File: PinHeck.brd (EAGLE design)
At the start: 359.2 x 152.3 mm, 309 parts, among them IC1 FT232RQ, IC2 PIC32MX7X5FL-PT, IC3 CD74HCT244E, IC4 CD74HCT244E, IC5 ULN2803A, J1 500075-1517, J11 No Load, J2 500075-1517, J6 161-3507-E, SW1 101-0134-EV, SW2 101-0134-EV, U1 P8X32A-Q44, U10 74HCT2G04GV,125, U11 74HC165D,652, U12 74HC165D,652, U13 MIC1232, U14 MC74HC08ADG, U15 MC74HC08ADG, U16 MC74HC08ADG, U17 MC74HC08ADG, U18 MC74HC08ADG, U19 MC74HC08ADG, U2 FT230X, U20 TIP107, U21 TIP107, U22 TIP107, U23 TIP107, U24 TIP107, U25 TIP107, U26 TIP107, U27 TIP107, U28 TIP102, U29 TIP102, U3 74HC595D-Q100, U30 TIP102, U31 TIP102, U32 TIP102, U33 TIP102, U34 TIP102, U35 TIP102, U36 WS2801, U37 TIP102, U38 WS2801, U4 CAT24M01XI-T2, U5 74HC595D-Q100, U6 74HC595D-Q100, U7 74HC595D-Q100, U8 74HC595D-Q100, U9 74HC595D-Q100, X1 FQ7050B-8.000, X2 ECS-65-20-4X

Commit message: Changed the alphanumeric display to be GI.
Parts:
- removed AN_J3, AN_J6, AN_J7: 26-60-4090, PP_Connectors:MOLEX_KK_9
- removed C27, C28, C29, C30, C31: .1uF, PP_Passives:0805
- removed MPU: (no value), PP_Connectors:HEADER_02X13_PTH
- added GI_0, GI_1: 26-60-4090, PP_Connectors:MOLEX_KK_9
- added R101, R103, R105, R107, R109, R111, R113, R125, R126, R127, R128, R129, R130, R131, R132, R99: 360, PP_Passives:0805
- added U40, U41, U42, U43, U44, U45, U46, U47, U48, U49, U50, U51: TIP102, PP_DiscreteSemi:TO-220AB
- SOL_0, SOL_1, SOL_10, SOL_11, SOL_12, SOL_13, SOL_14, SOL_15, SOL_16, SOL_17, SOL_18, SOL_19, SOL_2, SOL_20, SOL_21, SOL_22, SOL_23, SOL_3, SOL_4, SOL_5, SOL_6, SOL_7, SOL_8, SOL_9: value RFP12N10L -> IRL530
- U6, U7, U8, U9: value 74HC595D-Q100 -> TIP102; device PP_DigitalIC:SO-16 -> PP_DiscreteSemi:TO-220AB
- moved U5 35.2 mm to (308.6, 57.7), turned to 0 degrees
- moved U3 25.9 mm to (308.6, 98.6)
- moved C26 25.2 mm to (301.0, 57.1)
- moved U7 23.9 mm to (290.3, 80.5), turned to 90 degrees
- moved U8 23.9 mm to (296.7, 80.5), turned to 90 degrees
- moved C25 18.9 mm to (301.8, 99.3), turned to 90 degrees
- moved U6 12.7 mm to (284.0, 80.5), turned to 90 degrees
- moved U9 11.9 mm to (303.3, 80.5), turned to 90 degrees
- moved U10 8.44 mm to (289.1, 101.6), turned to 180 degrees
- moved U20 1.27 mm to (-5.59, 93.2)
- moved U22 1.27 mm to (4.06, 93.2)
- moved U24 1.27 mm to (13.7, 93.2)
- moved U26 1.27 mm to (23.4, 93.2)
- moved U28 1.02 mm to (-5.84, 48.3)
- moved U30 1.02 mm to (3.81, 48.3)
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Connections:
- net AN_DATA_COL renamed GI_DATA_COL
- net AN_DATA_COL_B renamed GI_DATA_COL_B
- removed net AN_J3_1: AN_J3.P$1, U5.7
- removed net AN_J3_2: AN_J3.P$2, U5.6
- removed net AN_J3_3: AN_J3.P$3, U5.5
- removed net AN_J3_4: AN_J3.P$4, U5.4
- removed net AN_J3_5: AN_J3.P$5, U5.3
- removed net AN_J3_6: AN_J3.P$6, U5.2
- removed net AN_J3_7: AN_J3.P$8, U5.1
- removed net AN_J3_8: AN_J3.P$9, U5.15
- removed net AN_J6_1: AN_J6.P$1, U3.7
- removed net AN_J6_2: AN_J6.P$2, U3.6
- removed net AN_J6_3: AN_J6.P$3, U3.5
- removed net AN_J6_4: AN_J6.P$4, U3.4
- removed net AN_J6_5: AN_J6.P$5, U3.3
- removed net AN_J6_6: AN_J6.P$6, U3.2
- removed net AN_J6_7: AN_J6.P$7, U3.1
- removed net AN_J6_8: AN_J6.P$9, U3.15
- removed net AN_J7_1: AN_J7.P$1, U6.15
- removed net AN_J7_2: AN_J7.P$2, U6.1
- removed net AN_J7_3: AN_J7.P$3, U6.2
- removed net AN_J7_4: AN_J7.P$4, U6.3
- removed net AN_J7_5: AN_J7.P$5, U6.4
- removed net AN_J7_6: AN_J7.P$7, U6.5
- removed net AN_J7_7: AN_J7.P$8, U6.6
- removed net AN_J7_8: AN_J7.P$9, U6.7
- removed net MPU_10: MPU.22, U7.15
- removed net MPU_11: MPU.6, U9.7
- removed net MPU_12: MPU.21, U9.6
- removed net MPU_13: MPU.7, U9.5
- removed net MPU_14: MPU.20, U9.4
- removed net MPU_15: MPU.8, U9.3
- removed net MPU_16: MPU.19, U9.2
- removed net MPU_17: MPU.9, U9.1
- removed net MPU_18: MPU.18, U9.15
- removed net MPU_19: MPU.10, U8.7
- removed net MPU_20: MPU.17, U8.6
- removed net MPU_21: MPU.11, U8.5
- removed net MPU_22: MPU.16, U8.4
- removed net MPU_23: MPU.12, U8.3
- removed net MPU_24: MPU.15, U8.2
- removed net MPU_25: MPU.13, U8.1
- removed net MPU_26: MPU.14, U8.15
- removed net MPU_3: MPU.2, U7.7
- removed net MPU_4: MPU.25, U7.6
- removed net MPU_5: MPU.3, U7.5
- removed net MPU_6: MPU.24, U7.4
- removed net MPU_7: MPU.4, U7.3
- removed net MPU_8: MPU.23, U7.2
- removed net MPU_9: MPU.5, U7.1
- removed net ROW_ONE_DATE_B: U8.9, U9.14
- removed net ROW_ZERO_DATA_B: U6.9, U7.14
- new net GI_0: R99.1, U3.15
- new net GI_1: R101.1, U3.1
- new net GI_10: R127.1, U5.2
- new net GI_11: R128.1, U5.3
- new net GI_12: R129.1, U5.4
- new net GI_13: R130.1, U5.5
- new net GI_14: R131.1, U5.6
- new net GI_15: R132.1, U5.7
- new net GI_2: R103.1, U3.2
- new net GI_3: R105.1, U3.3
- new net GI_4: R107.1, U3.4
- new net GI_5: R109.1, U3.5
- new net GI_6: R111.1, U3.6
- new net GI_7: R113.1, U3.7
- new net GI_8: R125.1, U5.15
- new net GI_9: R126.1, U5.1
- new net GI_R_0: GI_0.P$1, U6.D
- new net GI_R_1: GI_0.P$2, U7.D
- new net GI_R_10: GI_1.P$3, U46.D
- new net GI_R_11: GI_1.P$4, U47.D
- new net GI_R_12: GI_1.P$5, U48.D
- new net GI_R_13: GI_1.P$6, U49.D
- new net GI_R_14: GI_1.P$7, U50.D
- new net GI_R_15: GI_1.P$8, U51.D
- new net GI_R_2: GI_0.P$3, U8.D
- new net GI_R_3: GI_0.P$4, U9.D
- new net GI_R_4: GI_0.P$5, U40.D
- new net GI_R_5: GI_0.P$6, U41.D
- new net GI_R_6: GI_0.P$7, U42.D
- new net GI_R_7: GI_0.P$8, U43.D
- new net GI_R_8: GI_1.P$1, U44.D
- new net GI_R_9: GI_1.P$2, U45.D
- new net N$481: R99.2, U6.G
- new net N$482: R101.2, U7.G
- new net N$483: R103.2, U8.G
- new net N$484: R105.2, U9.G
- new net N$485: R107.2, U40.G
- new net N$486: R109.2, U41.G
- new net N$487: R111.2, U42.G
- new net N$488: R113.2, U43.G
- new net N$489: R125.2, U44.G
- new net N$490: R126.2, U45.G
- new net N$491: R127.2, U46.G
- new net N$492: R128.2, U47.G
- new net N$493: R129.2, U48.G
- new net N$494: R130.2, U49.G
- new net N$495: R131.2, U50.G
- new net N$496: R132.2, U51.G
- net !AN_BLANK: no longer MPU.1
- net !DATA_LAT: no longer U6.11, U7.11, U8.11, U9.11
- net 5V: now also GI_0.P$9, GI_1.P$9; no longer C27.2, C28.2, C29.2, C30.2, C31.2, U6.10, U6.16, U7.10, U7.16, U8.10, U8.16, U8.8, U9.10, U9.16
- net DATA_CLK: no longer U6.12, U7.12, U8.12, U9.12
- net GND: now also U40.S, U41.S, U42.S, U43.S, U44.S, U45.S, U46.S, U47.S, U48.S, U49.S, U50.S, U51.S, U6.S, U7.S, U8.S, U9.S; no longer C27.1, C28.1, C29.1, C30.1, C31.1, IC5.10, MPU.26, U6.13, U6.8, U7.13, U7.8, U8.13, U9.13, U9.8
- net ROW_ONE_DATA: no longer U8.14
- net ROW_ZERO_DATA: no longer U6.14
- net S_L: now also J6.2; no longer J6.5
- net S_R: now also J6.5; no longer J6.2
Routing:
- net ROW_ONE_DATA: track 223.5 -> 0.00 mm, vias 2 -> 0
- net ROW_ZERO_DATA: track 211.5 -> 0.00 mm, vias 2 -> 0
- net AN_J3_8: track 88.5 -> 0.00 mm
- net 5V: track 1019.5 -> 933.9 mm, vias 18 -> 14
- net AN_J6_8: track 79.6 -> 0.00 mm
- net AN_J3_7: track 76.3 -> 0.00 mm
- net GI_DATA_COL_B: track 21.1 -> 88.8 mm
- net AN_J3_6: track 66.8 -> 0.00 mm
- net AN_J6_7: track 64.5 -> 0.00 mm
- net AN_J3_5: track 61.3 -> 0.00 mm
- net AN_J6_6: track 60.0 -> 0.00 mm
- net AN_J7_8: track 59.5 -> 0.00 mm
- net AN_J7_7: track 59.2 -> 0.00 mm
- net AN_J7_6: track 57.3 -> 0.00 mm
- net AN_J6_5: track 55.5 -> 0.00 mm
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
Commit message: Changed Watchdog timer to work via 555timer
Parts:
- removed C49: .1uF, PP_Passives:0805
- removed U13: MIC1232, PP_FreqCtrl:SOIC-8
- added C27: EEE-1VA101XP, PP_Passives:6.3MM_CAP_SMD
- added D2: (no value), PP_Passives:SOD-128
- added P1: TC33X-2-103E, PP_Passives:TC33_TRIMMER
- added R133, R135: 10K, PP_Passives:0805
- added R134: 20K, PP_Passives:0805
- added U52: CD74HC123M96, PP_DigitalIC:SOIC-16
- moved R118 10.4 mm to (112.8, 73.4)
- moved WATCHDOG 8.13 mm to (115.6, 73.4), turned to 90 degrees
- moved C48 7.87 mm to (98.0, 86.4), turned to 0 degrees
- moved R3 1.02 mm to (104.6, 137.2)
- moved C17 0.76 mm to (271.0, 123.7)
- moved C8 0.51 mm to (104.6, 135.1)
- moved C10 0.25 mm to (96.0, 106.7)
- moved C5 0.25 mm to (98.0, 106.7)
- flipped J6 to the top
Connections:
- new net N$497: P1.2, R134.1
- new net WATCHDOG_ADJUST: C27.POS, D2.ANODE, P1.3, U52.15
- net 5V: now also D2.CATHODE, R134.2, U52.16, U52.2, U52.3; no longer C49.1, U13.2, U13.3, U13.8
- net GND: now also C27.NEG, R133.2, R135.2, U52.14, U52.8; no longer C49.2, U13.4
- net PIC_ENABLE: now also R133.1, U52.1; no longer U13.7
- net S_L: now also J6.5; no longer J6.2
- net S_R: now also J6.2; no longer J6.5
- net WATCHDOG: now also R135.1, U52.13; no longer U13.6
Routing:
- net WATCHDOG_ADJUST: track 0.00 -> 23.6 mm
- net 5V: track 933.9 -> 949.3 mm, vias 14 -> 15
- net PIC_ENABLE: track 49.3 -> 62.5 mm
- net S_L: track 36.7 -> 41.3 mm
- net N$497: track 0.00 -> 3.87 mm
- net N$50: track 5.25 -> 3.48 mm
- net WATCHDOG: track 329.2 -> 330.8 mm
- net S_R: track 41.5 -> 40.2 mm
- net AVCC: track 11.1 -> 12.1 mm
- net RES: track 11.9 -> 12.6 mm
- net RTS: track 49.0 -> 48.2 mm
- net 3.3V: track 1201.0 -> 1201.5 mm

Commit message: Fixing some layout issues. Added some breakouts.
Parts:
- added J3: (no value), PP_Connectors:HEADER_01X04_PTH
- added R136: 0, PP_Passives:0805
- D2: value (none) -> CGRM4001-HF; device PP_Passives:SOD-128 -> PP_Passives:SOD-123
- renumbered SUPER_AUX_CON to TCBTWDN
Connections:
- net !AN_BLANK: now also J3.4
- net 5V: now also D2.1; no longer D2.CATHODE
- net GND: now also J3.2, J3.3, R136.1
- net SOL_GND: now also R136.2
- net WATCHDOG: now also J3.1
- net WATCHDOG_ADJUST: now also D2.2; no longer D2.ANODE
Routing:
- net WATCHDOG: track 330.8 -> 343.2 mm, vias 21 -> 22
- net SOL_GND: track 294.5 -> 302.7 mm
- net !AN_BLANK: track 0.00 -> 4.73 mm
- net DATA_CLK: track 369.7 -> 365.2 mm, vias 5 -> 4
- net N$487: track 11.0 -> 12.5 mm
- net N$486: track 7.70 -> 9.19 mm
- net 5V: track 949.3 -> 950.2 mm
- net WATCHDOG_ADJUST: track 23.6 -> 24.1 mm
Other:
- board text added: "AN_"
- board text added: "WD"

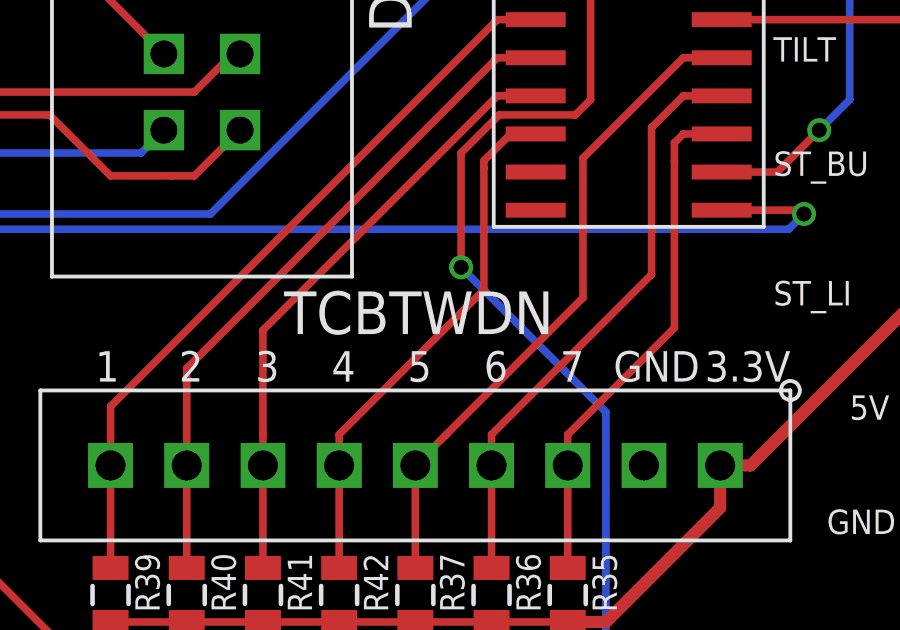
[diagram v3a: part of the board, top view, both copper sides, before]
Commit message: changed port name. added new layout pic.
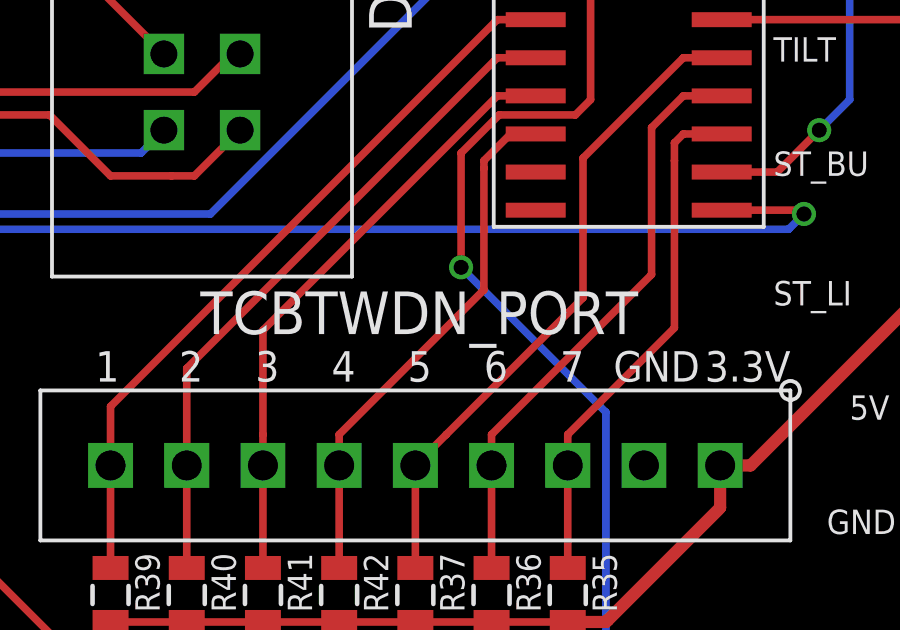
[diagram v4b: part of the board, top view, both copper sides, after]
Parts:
- renumbered TCBTWDN to TCBTWDN_PORT
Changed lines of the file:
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@@
 <attribute name="NAME" x="111.379" y="74.9935" size="0.8128" layer="25" font="vector"/>
 </element>
-<element name="TCBTWDN" library="PP_Connectors" package="HEADER_01X09_PTH" value="" x="303.276" y="113.284" smashed="yes" rot="R180">
-<attribute name="NAME" x="298.904" y="117.662" size="1.4224" layer="21" font="vector"/>
+<element name="TCBTWDN_PORT" library="PP_Connectors" package="HEADER_01X09_PTH" value="" x="303.276" y="113.284" smashed="yes" rot="R180">
+<attribute name="NAME" x="296.11" y="117.662" size="1.4224" layer="21" font="vector"/>
 </element>
 <element name="U36" library="PP_DigitalIC" package="SOP-14" value="WS2801" x="167.64" y="138.938" rot="R180"/>
@@
 <contactref element="R117" pad="1"/>
 <contactref element="R118" pad="2"/>
-<contactref element="TCBTWDN" pad="2"/>
+<contactref element="TCBTWDN_PORT" pad="2"/>
 <contactref element="U38" pad="7"/>
 <contactref element="U36" pad="7"/>
@@
 <contactref element="PSU_PWR" pad="A"/>
 <contactref element="AUX_PORT" pad="P$6"/>
-<contactref element="TCBTWDN" pad="1"/>
+<contactref element="TCBTWDN_PORT" pad="1"/>
 <contactref element="U38" pad="14"/>
 <contactref element="U36" pad="14"/>
@@
 <contactref element="U11" pad="6"/>
 <contactref element="R42" pad="1"/>
-<contactref element="TCBTWDN" pad="6"/>
+<contactref element="TCBTWDN_PORT" pad="6"/>
 <wire x1="300.736" y1="113.284" x2="300.736" y2="114.3135" width="0.254" layer="1"/>
 <wire x1="300.736" y1="109.866" x2="300.736" y2="113.284" width="0.254" layer="1"/>
@@
 <contactref element="U11" pad="5"/>
 <contactref element="R41" pad="1"/>
-<contactref element="TCBTWDN" pad="7"/>
+<contactref element="TCBTWDN_PORT" pad="7"/>
 <wire x1="307.288" y1="125.603" x2="306.0085" y2="125.603" width="0.254" layer="1"/>
 <wire x1="298.196" y1="113.284" x2="298.196" y2="114.3135" width="0.254" layer="1"/>
@@
 <contactref element="U11" pad="4"/>
 <contactref element="R40" pad="1"/>
-<contactref element="TCBTWDN" pad="8"/>
+<contactref element="TCBTWDN_PORT" pad="8"/>
 <wire x1="307.288" y1="126.873" x2="306.0085" y2="126.873" width="0.254" layer="1"/>
 <wire x1="306.0085" y1="126.873" x2="295.656" y2="116.5205" width="0.254" layer="1"/>
@@
 <contactref element="U11" pad="3"/>
 <contactref element="R39" pad="1"/>
-<contactref element="TCBTWDN" pad="9"/>
+<contactref element="TCBTWDN_PORT" pad="9"/>
 <wire x1="307.288" y1="128.143" x2="306.0085" y2="128.143" width="0.254" layer="1"/>
 <wire x1="306.0085" y1="128.143" x2="293.116" y2="115.2505" width="0.254" layer="1"/>
@@
 <contactref element="U11" pad="12"/>
 <contactref element="R36" pad="1"/>
-<contactref element="TCBTWDN" pad="4"/>
+<contactref element="TCBTWDN_PORT" pad="4"/>
 <wire x1="305.816" y1="113.284" x2="305.816" y2="114.3135" width="0.254" layer="1"/>
 <wire x1="313.488" y1="125.603" x2="312.2085" y2="125.603" width="0.254" layer="1"/>
@@
 <contactref element="U11" pad="11"/>
 <contactref element="R35" pad="1"/>
-<contactref element="TCBTWDN" pad="3"/>
+<contactref element="TCBTWDN_PORT" pad="3"/>
 <wire x1="313.488" y1="124.333" x2="312.2085" y2="124.333" width="0.254" layer="1"/>
 <wire x1="308.356" y1="113.284" x2="308.356" y2="114.3135" width="0.254" layer="1"/>
@@
 <contactref element="U11" pad="13"/>
 <contactref element="R37" pad="1"/>
-<contactref element="TCBTWDN" pad="5"/>
+<contactref element="TCBTWDN_PORT" pad="5"/>
 <wire x1="313.488" y1="126.873" x2="312.2085" y2="126.873" width="0.254" layer="1"/>
 <wire x1="303.276" y1="109.866" x2="303.276" y2="113.284" width="0.254" layer="1"/>

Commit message: New Spooky Logo
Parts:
- added LOGO1: SPOOKY_LOGOSPOOKY_LOGO, PP_Aesthetics:SPOOKY_LOGO
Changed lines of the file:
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@@
 <element name="J3" library="PP_Connectors" package="HEADER_01X04_PTH" value="" x="277.622" y="98.044"/>
 <element name="R136" library="PP_Passives" package="0805" value="0" x="237.49" y="70.866" rot="R270"/>
+<element name="LOGO1" library="PP_Aesthetics" package="SPOOKY_LOGO" value="SPOOKY_LOGOSPOOKY_LOGO" x="37.338" y="123.698"/>
 </elements>
 <signals>
